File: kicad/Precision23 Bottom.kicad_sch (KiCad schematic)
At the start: 14 parts, among them J396 STANDOFF, J397 STANDOFF, J398 STANDOFF, J399 STANDOFF, J503 Conn_02x03_Odd_Even, J504 Conn_01x06, J507 Conn_01x06, J509 Conn_01x02_Pin, J895 USB A Male to Blank

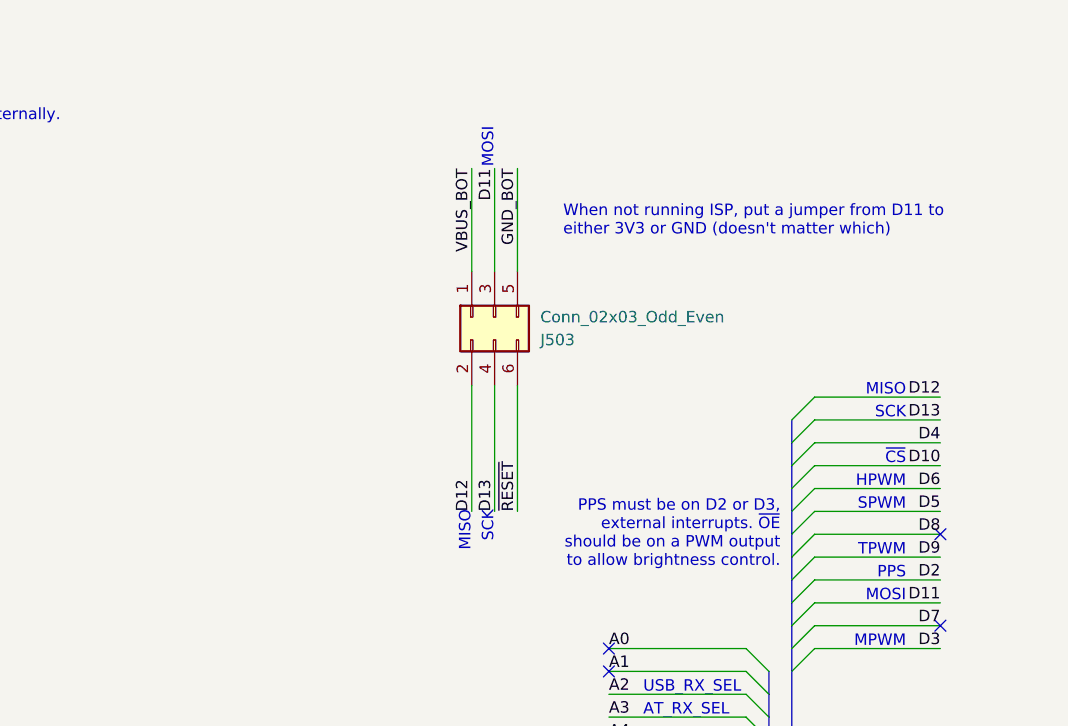
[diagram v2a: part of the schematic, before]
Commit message: Refactored board, put 5V0 on all parts except GPS
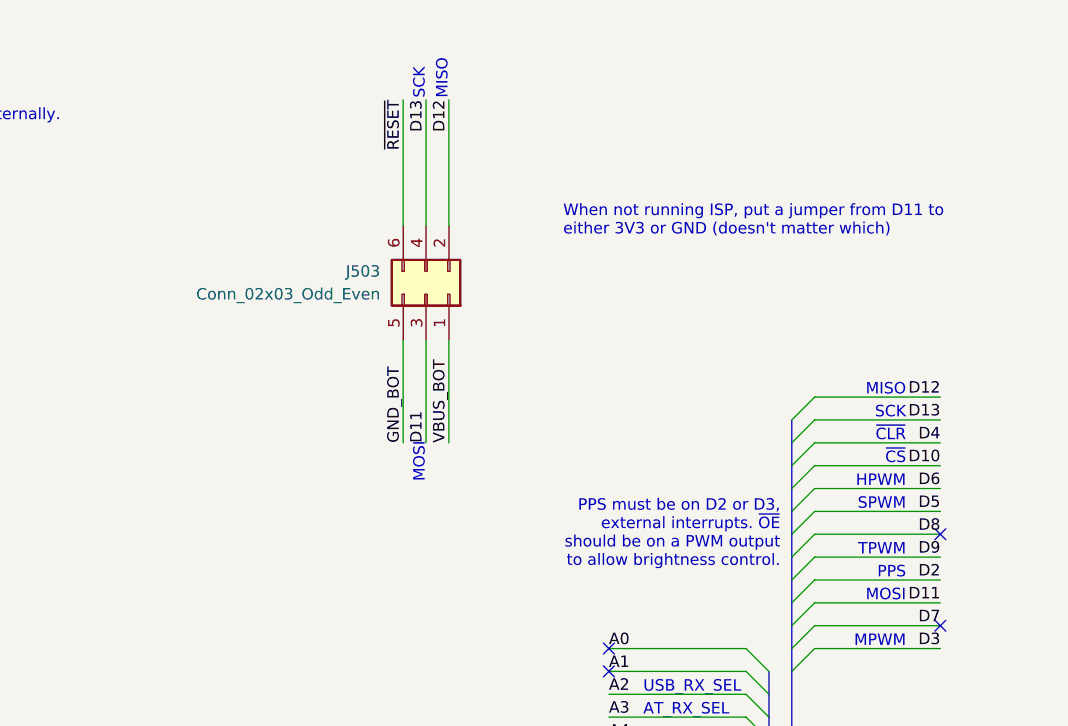
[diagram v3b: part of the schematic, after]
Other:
- note added: "~{CLR}"
- moved on the sheet: J503
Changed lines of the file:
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@@
     (stroke (width 0) (type default))
   )
-  (wire (pts (xy 124.46 33.02) (xy 124.46 44.45))
+  (wire (pts (xy 116.84 63.5) (xy 116.84 52.07))
     (stroke (width 0) (type default))
   )
@@
     (stroke (width 0) (type default))
   )
-  (wire (pts (xy 121.92 57.15) (xy 121.92 71.12))
-    (stroke (width 0) (type default))
-  )
-  (wire (pts (xy 121.92 33.02) (xy 121.92 44.45))
+  (wire (pts (xy 119.38 39.37) (xy 119.38 25.4))
+    (stroke (width 0) (type default))
+  )
+  (wire (pts (xy 119.38 63.5) (xy 119.38 52.07))
     (stroke (width 0) (type default))
   )
@@
     (stroke (width 0) (type default))
   )
-  (wire (pts (xy 127 57.15) (xy 127 71.12))
+  (wire (pts (xy 114.3 39.37) (xy 114.3 25.4))
     (stroke (width 0) (type default))
   )
@@
     (stroke (width 0) (type default))
   )
-  (wire (pts (xy 124.46 57.15) (xy 124.46 71.12))
+  (wire (pts (xy 116.84 39.37) (xy 116.84 25.4))
     (stroke (width 0) (type default))
   )
@@
     (stroke (width 0) (type default))
   )
-  (wire (pts (xy 127 33.02) (xy 127 44.45))
+  (wire (pts (xy 114.3 63.5) (xy 114.3 52.07))
     (stroke (width 0) (type default))
   )
@@
     (effects (font (size 1.27 1.27)) (justify right bottom))
   )
-  (text "MISO" (at 121.92 71.12 90)
-    (effects (font (size 1.27 1.27)) (justify right bottom))
+  (text "MISO" (at 119.38 25.4 90)
+    (effects (font (size 1.27 1.27)) (justify left bottom))
   )
   (text "MPWM" (at 170.18 86.36 0)
@@
     (effects (font (size 1.27 1.27)) (justify right bottom))
   )
-  (text "MOSI" (at 124.46 33.02 90)
-    (effects (font (size 1.27 1.27)) (justify left bottom))
+  (text "MOSI" (at 116.84 63.5 90)
+    (effects (font (size 1.27 1.27)) (justify right bottom))
   )
   (text "FT232 interface" (at 50.165 183.515 0)
@@
     (effects (font (size 1.27 1.27)) (justify right bottom))
   )
-  (text "SCK" (at 124.46 71.12 90)
-    (effects (font (size 1.27 1.27)) (justify right bottom))
+  (text "SCK" (at 116.84 25.4 90)
+    (effects (font (size 1.27 1.27)) (justify left bottom))
   )
   (text "Use hardware SPI to do the shift-out.\nIf we can't get that to work, we can still\nbit-bang on these lines just as easily\nas any other."
@@
     (effects (font (size 1.27 1.27)) (justify right bottom))
   )
+  (text "~{CLR}" (at 170.18 63.5 0)
+    (effects (font (size 1.27 1.27)) (justify right bottom))
+  )
   (label "A3" (at 114.3 101.6 180) (fields_autoplaced)
     (effects (font (size 1.27 1.27)) (justify right bottom))
@@
     (effects (font (size 1.27 1.27)) (justify right bottom))
   )
-  (label "~{RESET}" (at 127 71.12 90) (fields_autoplaced)
-    (effects (font (size 1.27 1.27)) (justify left bottom))
+  (label "~{RESET}" (at 114.3 25.4 270) (fields_autoplaced)
+    (effects (font (size 1.27 1.27)) (justify right bottom))
   )
   (label "D11" (at 173.99 81.28 180) (fields_autoplaced)
@@
     (effects (font (size 1.27 1.27)) (justify left bottom))
   )
-  (label "D12" (at 121.92 71.12 90) (fields_autoplaced)
-    (effects (font (size 1.27 1.27)) (justify left bottom))
+  (label "D12" (at 119.38 25.4 270) (fields_autoplaced)
+    (effects (font (size 1.27 1.27)) (justify right bottom))
   )
   (label "D10" (at 41.91 44.45 0) (fields_autoplaced)
@@
     (effects (font (size 1.27 1.27)) (justify left bottom))
   )
-  (label "D11" (at 124.46 33.02 270) (fields_autoplaced)
-    (effects (font (size 1.27 1.27)) (justify right bottom))
+  (label "D11" (at 116.84 63.5 90) (fields_autoplaced)
+    (effects (font (size 1.27 1.27)) (justify left bottom))
   )
   (label "D4" (at 177.8 107.95 0) (fields_autoplaced)
@@
     (effects (font (size 1.27 1.27)) (justify right bottom))
   )
-  (label "D13" (at 124.46 71.12 90) (fields_autoplaced)
-    (effects (font (size 1.27 1.27)) (justify left bottom))
+  (label "D13" (at 116.84 25.4 270) (fields_autoplaced)
+    (effects (font (size 1.27 1.27)) (justify right bottom))
   )
   (label "A2" (at 114.3 121.92 180) (fields_autoplaced)
@@
     (effects (font (size 1.27 1.27)) (justify left bottom))
   )
-  (label "GND_BOT" (at 127 33.02 270) (fields_autoplaced)
-    (effects (font (size 1.27 1.27)) (justify right bottom))
+  (label "GND_BOT" (at 114.3 63.5 90) (fields_autoplaced)
+    (effects (font (size 1.27 1.27)) (justify left bottom))
   )
   (label "D13" (at 177.8 105.41 0) (fields_autoplaced)
@@
     (effects (font (size 1.27 1.27)) (justify right bottom))
   )
-  (label "VBUS_BOT" (at 121.92 33.02 270) (fields_autoplaced)
-    (effects (font (size 1.27 1.27)) (justify right bottom))
+  (label "VBUS_BOT" (at 119.38 63.5 90) (fields_autoplaced)
+    (effects (font (size 1.27 1.27)) (justify left bottom))
   )
   (label "D4" (at 173.99 63.5 180) (fields_autoplaced)
@@
     )
   )
-  (symbol (lib_id "Connector_Generic:Conn_02x03_Odd_Even") (at 124.46 49.53 90) (mirror x) (unit 1)
+  (symbol (lib_id "Connector_Generic:Conn_02x03_Odd_Even") (at 116.84 46.99 270) (mirror x) (unit 1)
     (in_bom yes) (on_board yes) (dnp no)
-    (property "Reference" "J503" (at 129.54 52.07 90)
+    (property "Reference" "J503" (at 111.76 44.45 90)
       (effects (font (size 1.27 1.27)) (justify right))
     )
-    (property "Value" "Conn_02x03_Odd_Even" (at 129.54 49.53 90)
+    (property "Value" "Conn_02x03_Odd_Even" (at 111.76 46.99 90)
       (effects (font (size 1.27 1.27)) (justify right))
     )
-    (property "Footprint" "Connector_PinSocket_2.54mm:PinSocket_2x03_P2.54mm_Vertical_SMD" (at 124.46 49.53 0)
+    (property "Footprint" "Connector_PinSocket_2.54mm:PinSocket_2x03_P2.54mm_Vertical_SMD" (at 116.84 46.99 0)
       (effects (font (size 1.27 1.27)) hide)
     )
-    (property "Datasheet" "https://gct.co/files/specs/2.54mm-socket-spec.pdf" (at 124.46 49.53 0)
+    (property "Datasheet" "https://gct.co/files/specs/2.54mm-socket-spec.pdf" (at 116.84 46.99 0)
       (effects (font (size 1.27 1.27)) hide)
     )
-    (property "Digikey" "2073-BG120-06-A-0-N-D-ND" (at 124.46 49.53 0)
+    (property "Digikey" "2073-BG120-06-A-0-N-D-ND" (at 116.84 46.99 0)
       (effects (font (size 1.27 1.27)) hide)
     )
-    (property "Part Number" "BG120-06-A-0-N-D" (at 124.46 49.53 0)
+    (property "Part Number" "BG120-06-A-0-N-D" (at 116.84 46.99 0)
       (effects (font (size 1.27 1.27)) hide)
     )
-    (property "Purpose" "ISP connector" (at 124.46 49.53 0)
+    (property "Purpose" "ISP connector" (at 116.84 46.99 0)
       (effects (font (size 1.27 1.27)) hide)
     )

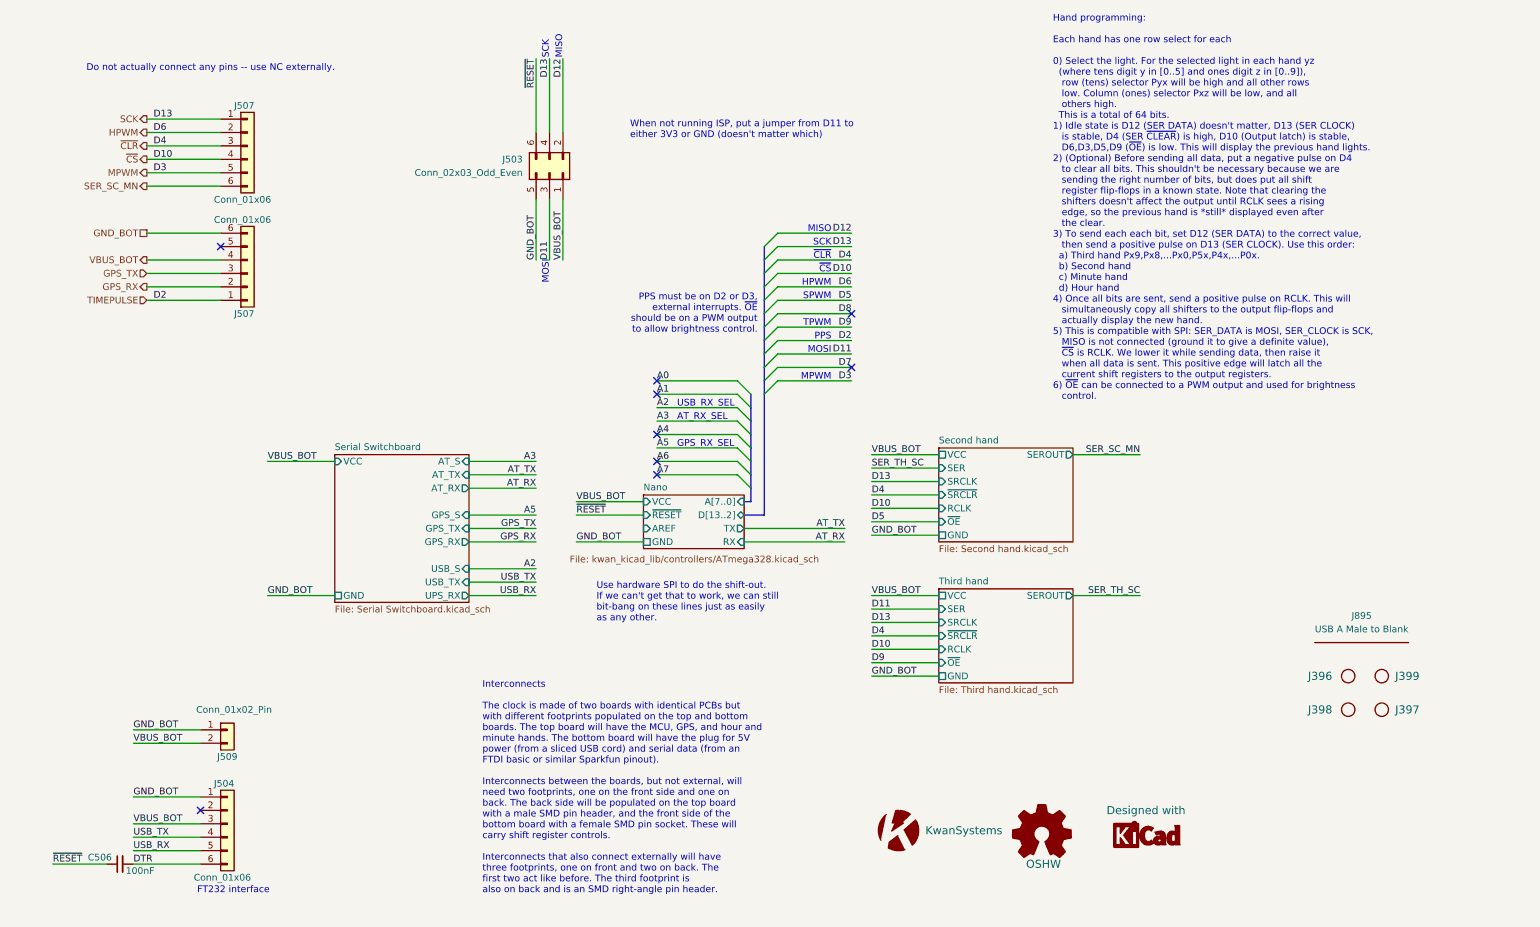
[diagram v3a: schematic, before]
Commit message: Put MOSFET switch transistors in place. We won't end up using these.
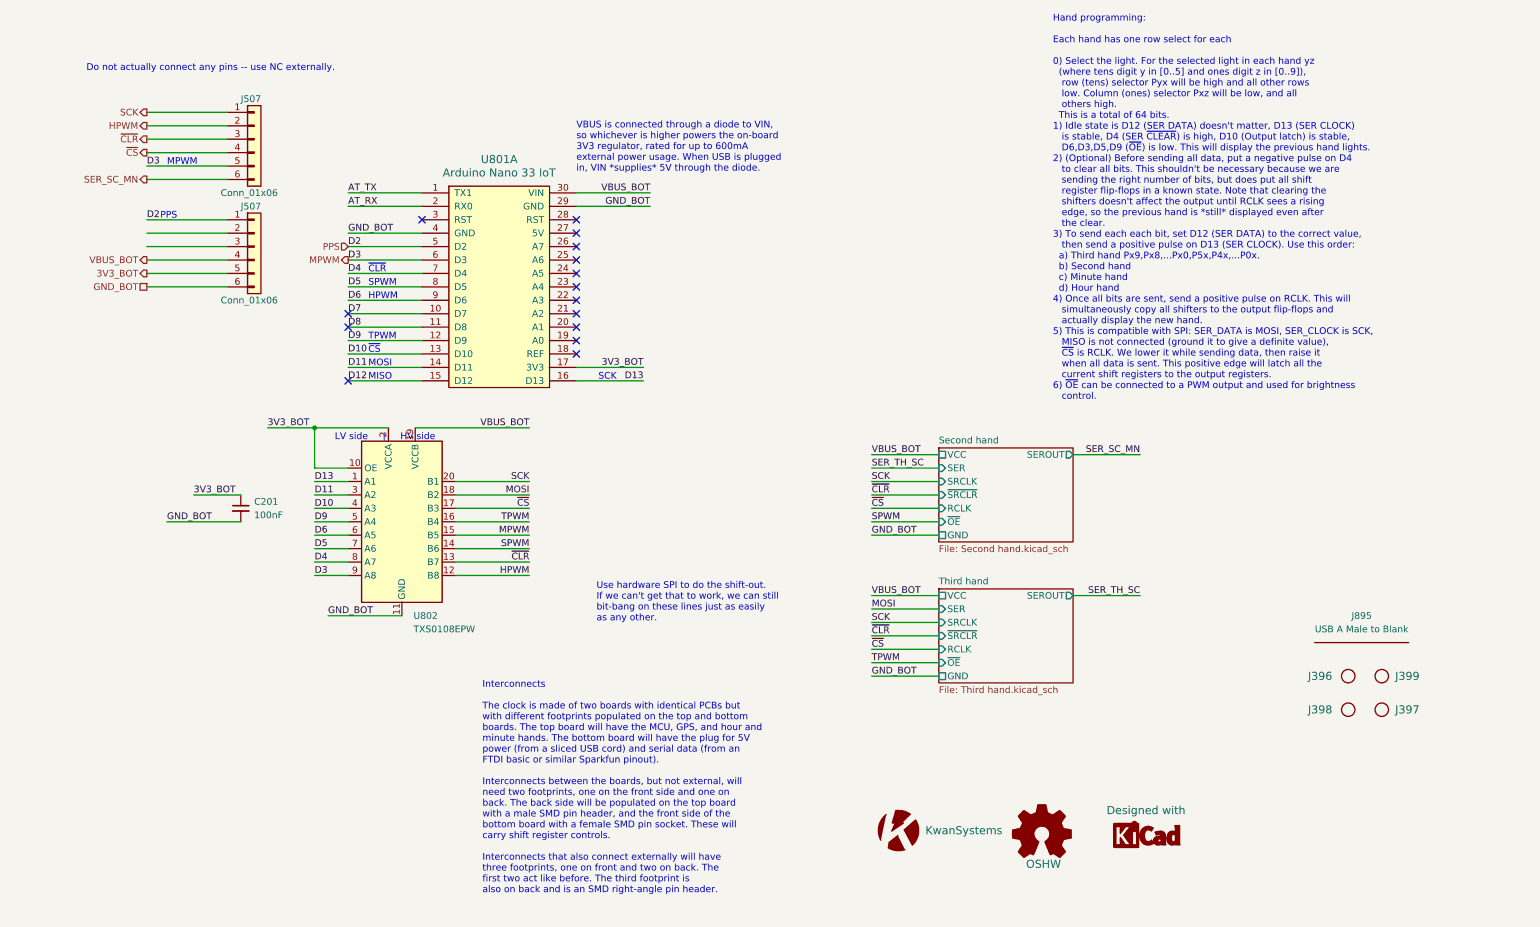
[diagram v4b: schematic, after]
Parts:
- removed C506: 100nF, Capacitor_SMD:C_0603_1608Metric, symbol Device:C_Small
- removed J503: Conn_02x03_Odd_Even, Connector_PinSocket_2.54mm:PinSocket_2x03_P2.54mm_Vertical_SMD, symbol Connector_Generic:Conn_02x03_Odd_Even
- removed J504: Conn_01x06, KwanSystems:SAMTEC_TSM-106-01-T-SH, symbol Connector_Generic:Conn_01x06
- removed J509: Conn_01x02_Pin, KwanSystems:SAMTEC_TSM-102-01-T-SH, symbol Connector_Generic:Conn_01x02
- added C201: 100nF, Capacitor_SMD:C_0603_1608Metric, symbol Device:C_Small
- added U801: Arduino Nano 33 IoT, KwanSystems:NanoCastellated, symbol KwanSystems:Arduino_Nano
- added U802: TXS0108EPW, Package_SO:TSSOP-20_4.4x6.5mm_P0.65mm, symbol Logic_LevelTranslator:TXS0108EPW
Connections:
- net AT_RX: now also U801.2 (RX0)
- net AT_TX: now also U801.1 (TX1)
- net D11: now also U801.14 (D11), U802.3 (A2)
- net D12: now also U801.15 (D12)
- net D5: now also U801.8 (D5), U802.7 (A6)
- net D7: now also U801.10 (D7)
- net D8: now also U801.11 (D8)
- net D9: now also U801.12 (D9), U802.5 (A4)
- net GND_BOT: now also C201.2, U801.29 (GND), U801.4 (GND), U802.11 (GND)
- net HPWM: now also U802.12 (B8)
- net MPWM: now also U801.6 (D3), U802.15 (B5), U802.9 (A8)
- net SCK: now also U802.20 (B1)
- net VBUS_BOT: now also U801.30 (VIN), U802.19 (VCCB)
- net ~{CLR}: now also U802.13 (B7)
- net ~{CS}: now also U802.17 (B3)
- net 3V3_BOT: now reaches J507.5 (Pin_5)
- net 3V3_BOT: now also C201.1, U801.17 (3V3), U802.10 (OE), U802.2 (VCCA)
- net GPS_RX: no longer names the net of J507.2 (Pin_2)
- net GPS_TX: no longer names the net of J507.3 (Pin_3)
- net TIMEPULSE renamed PPS
- net PPS: now also U801.5 (D2)
- new net D10: U801.13 (D10), U802.4 (A3)
- new net D13: U801.16 (D13), U802.1 (A1)
- new net D4: U801.7 (D4), U802.8 (A7)
- new net D6: U801.9 (D6), U802.6 (A5)
- new net MOSI: U802.18 (B2)
- new net SPWM: U802.14 (B6)
- new net TPWM: U802.16 (B4)
- no-connect marks 9 -> 15
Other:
- removed sheet Nano
- removed sheet Serial Switchboard
- note added: "LV side | HV side"
- note added: "VBUS is connected through a diode to VIN, so whichever is higher powers the on-board 3V3 regulator, rated for up to 600mA external power usage. When USB is plugged in, VIN *supplies* 5V through the diode."
- note removed: "AT_RX_SEL"
- note removed: "FT232 interface"
- note removed: "GPS_RX_SEL"
- note removed: "PPS must be on D2 or D3, external interrupts. ~{OE} should be on a PWM output to allow brightness control."
- note removed: "USB_RX_SEL"
- note removed: "When not running ISP, put a jumper from D11 to either 3V3 or GND (doesn't matter which)"
- moved on the sheet: J507
